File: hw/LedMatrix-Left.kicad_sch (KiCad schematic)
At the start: 76 parts, among them Q3200 DTA114E, Q3201 DTA114E, Q3202 DTA114E, Q3203 DTA114E, Q3204 DTA114E, Q3205 DTA114E, Q3206 DTA114E, Q3207 DTA114E, Q3208 DTA114E, Q3209 DTA114E, Q3210 DTC114EE, Q3211 DTC114EE, Q3212 DTC114EE, Q3213 DTC114EE, Q3214 DTC114EE, Q3215 DTC114EE, Q3216 DTC114EE, Q3217 DTC114EE, Q3218 DTC114EE, Q3219 DTC114EE, Q3220 DTC114EE, Q3221 DTC114EE, X3200 Lightpipe-5x5mm-Dome, X3201 Lightpipe-5x5mm-Dome

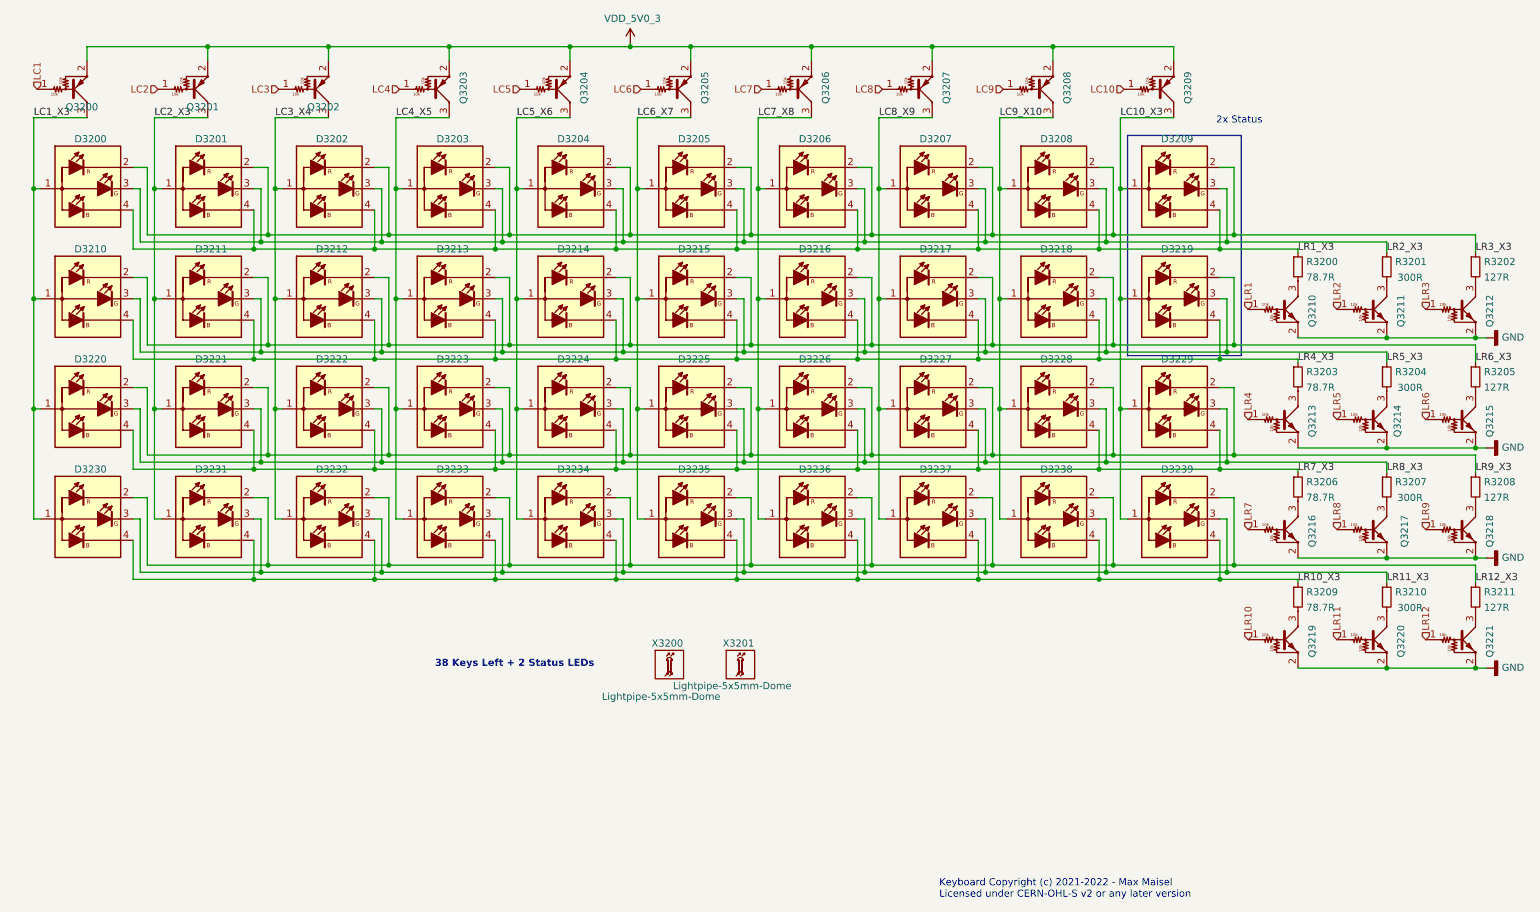
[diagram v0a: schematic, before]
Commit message: Replace LED matrix BJTs with MOSFETs and update PCB.
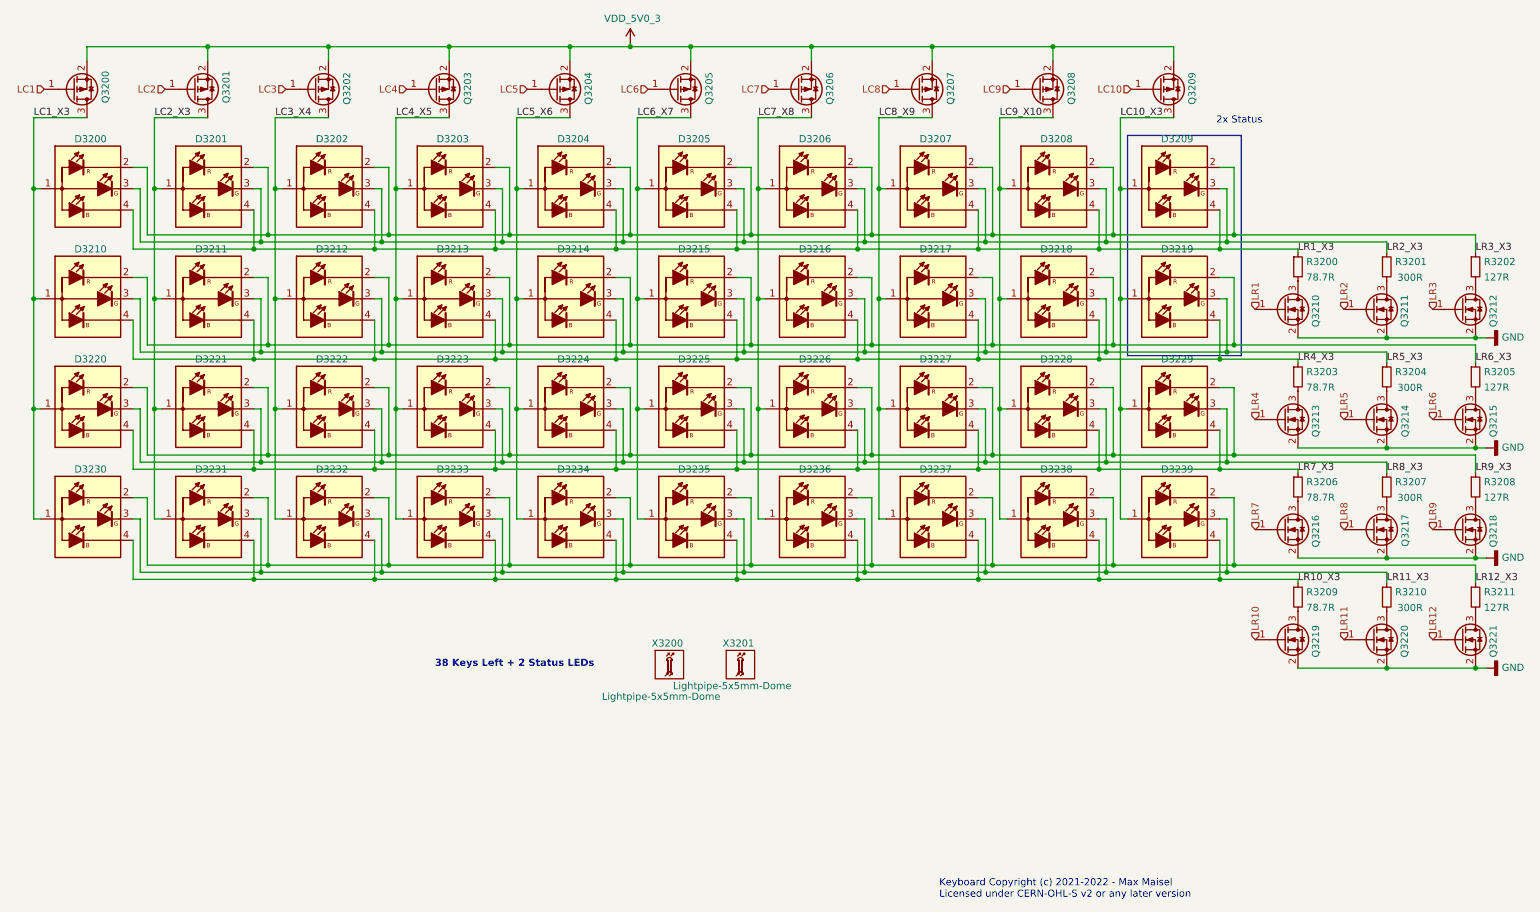
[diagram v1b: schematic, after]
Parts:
- Q3200, Q3201, Q3202, Q3203, Q3204, Q3205, Q3206, Q3207, Q3208, Q3209: value DTA114E -> NTA4151P; symbol Keyboard:DTA114E -> Keyboard:NTA4151PT1G; farnell# (none) -> 2317622; mouser# (none) -> 863-NTA4151PT1G
- Q3210, Q3211, Q3212, Q3213, Q3214, Q3215, Q3216, Q3217, Q3218, Q3219, Q3220, Q3221: value DTC114EE -> NTA4153N; symbol Keyboard:DTC114EE -> Keyboard:NTA4153NT1G; farnell# (none) -> 2317621; mouser# 863-DTC114EET1G -> 863-NTA4153NT1G
